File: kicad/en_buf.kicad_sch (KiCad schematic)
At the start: 2 parts, among them U1 74AHCT1G125

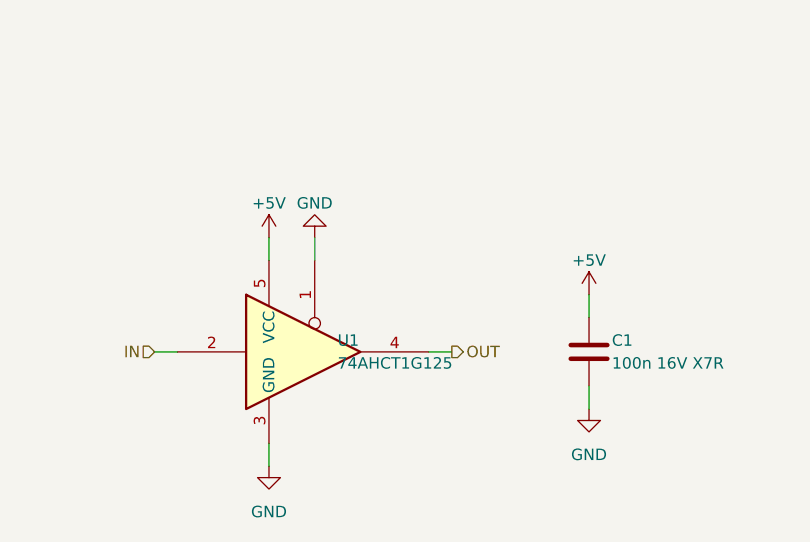
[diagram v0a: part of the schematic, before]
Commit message: Block-diagram top page, power review fixes, readable sheets
Top level
- Page 1 is now a block diagram of the signal flow (FPGA -> headers ->
  clock buffers / TX drive -> transceivers -> ADCs -> FPGA, mics, power).
- New group sheets hold the reused cells: tx (16 tx_group + 4 en_buf),
  array (64 channel), adcs (8 adc), mics (8 mic), clocks (7 clk_buf).
  Power and headers stay directly under the top. All written by gen_top.py,
  which now also survives a kicad-cli re-save of a cell sheet.

Power (review findings)
- Polyfuse 1812L200/16DR (16 V), TPS65131RGER stated explicitly, input caps
  2 x 10u 1206, 50 V caps on 12 V, inductor values carry minimum Isat.
- +3V3: TLV75733P (ceramic-stable) replaces TLV1117-33.
- New JP5/JP6 isolate +-6V5; every rail: REG node -> jumper -> rail with TP,
  LED (not on analog LDOs) and PWR_FLAG.
- Power sheet is now generated by build_cells.py in a 2x3 block layout
  (build_power.py removed).

Readability and small fixes
- Rails on sideways pins use labelled flags; sideways GND symbols hide text.
- tx_group: 595 outputs wired straight to the drivers.
- Title blocks on every sheet; channel sheet notes and field placement fixed
  (sch_fields.py --only, sch_annotate.py).
- ADC_SDI 10k pull-down, ADC reset/DOUT notes, mic cap 50 V.
- ERC 0 violations, 1,704 parts. PDFs: docs/schematics/00..13.
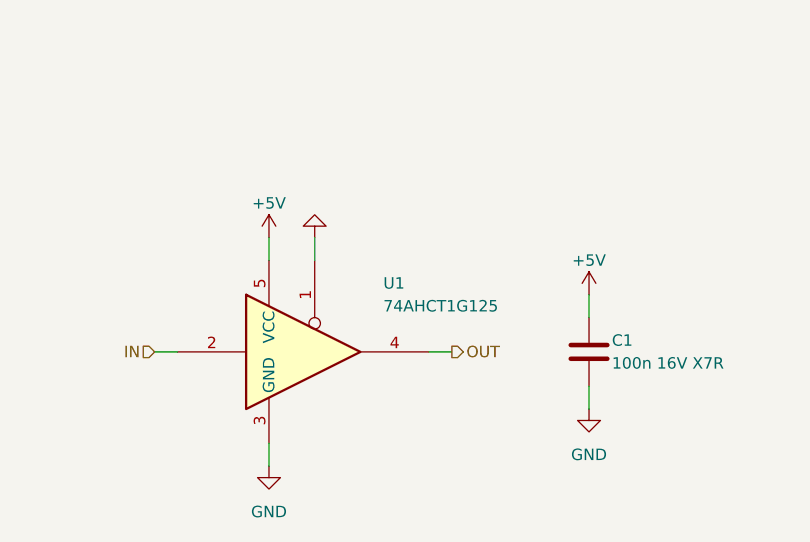
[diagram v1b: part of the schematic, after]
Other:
- company: (none) -> Hybrid 8x8 ultrasonic AESA
- title: (none) -> TX enable buffer (x4): 74AHCT1G125

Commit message: Optimized, costed BOM with LCSC numbers for every part
scripts/bom.py picks parts (Basic first, stock margin) and writes docs/bom.md,
fab/bom_jlcpcb.csv and scripts/parts.json; sch_lcsc.py fills LCSC fields from it.
Part changes: TPS7A4700RGWT for the out-of-stock TPS7A4701, BAV99 C2500, SS54 in SMA,
SMD1812P200TF16 polyfuse, 600R ferrite, Basic-value +5V/VDRV dividers (VDRV 15.4 V),
Sunlord SWPA6045 footprints, mic 100 nF C0G in 1206. AD7606C-16 and SPH0641 now
assembled by JLCPCB.
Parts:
- C1: LCSC TBD -> C14663
- U1: LCSC TBD -> C7484
